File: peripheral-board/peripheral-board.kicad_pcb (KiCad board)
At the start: 2 copper layers, 165 x 130 mm, 261 parts, among them CON4001 BARREL_JACK, CON8001 SD_Card, J10001 DB15_FEMALE_HighDensity, J7001 FCR1295, P10001 VGA, P1001 Peripheral Bus, P1002 Power, Q4001 IRLML2244TRPbF, Q5001 IRLML2244TRPbF, Q5002 IRLML2244TRPbF, Q8001 BSS84LT1G, SW1001 Power, SW2001 1, SW2002 2, SW2003 3, SW2004 4, SW2005 5, SW2006 6, SW2007 7, SW2008 8, SW2009 9, SW2010 0, SW2011 +, SW2012 ´, SW2013 BKSP, SW2014 TROLL, SW2015 §, SW2016 UP, SW2017 RMB, SW2018 Q, SW2019 W, SW2020 E, SW2021 R, SW2022 T, SW2023 Y, SW2024 U, SW2025 I, SW2026 O, SW2027 P, SW2028 Å, SW2029 ¨, SW2030 RETURN, SW2031 ALT_GR, SW2032 <, SW2033 LEFT, SW2034 MMB, SW2035 A, SW2036 S, SW2037 D, SW2038 F, SW2039 G, SW2040 H, SW2041 J, SW2042 K, SW2043 L, SW2044 Ö, SW2045 Ä, SW2046 ', SW2047 ESC, SW2048 TAB, SW2049 ALT, SW2050 DOWN, SW2051 LMB, SW2052 SHIFT_L, SW2053 Z, SW2054 X, SW2055 C, SW2056 V, SW2057 B, SW2058 N, SW2059 M, SW2060 ,, SW2061 ., SW2062 -, SW2063 SHIFT_R, SW2064 FN_R, SW2065 SPACE, SW2066 FN_L, SW2067 RIGHT, SW2068 CTRL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

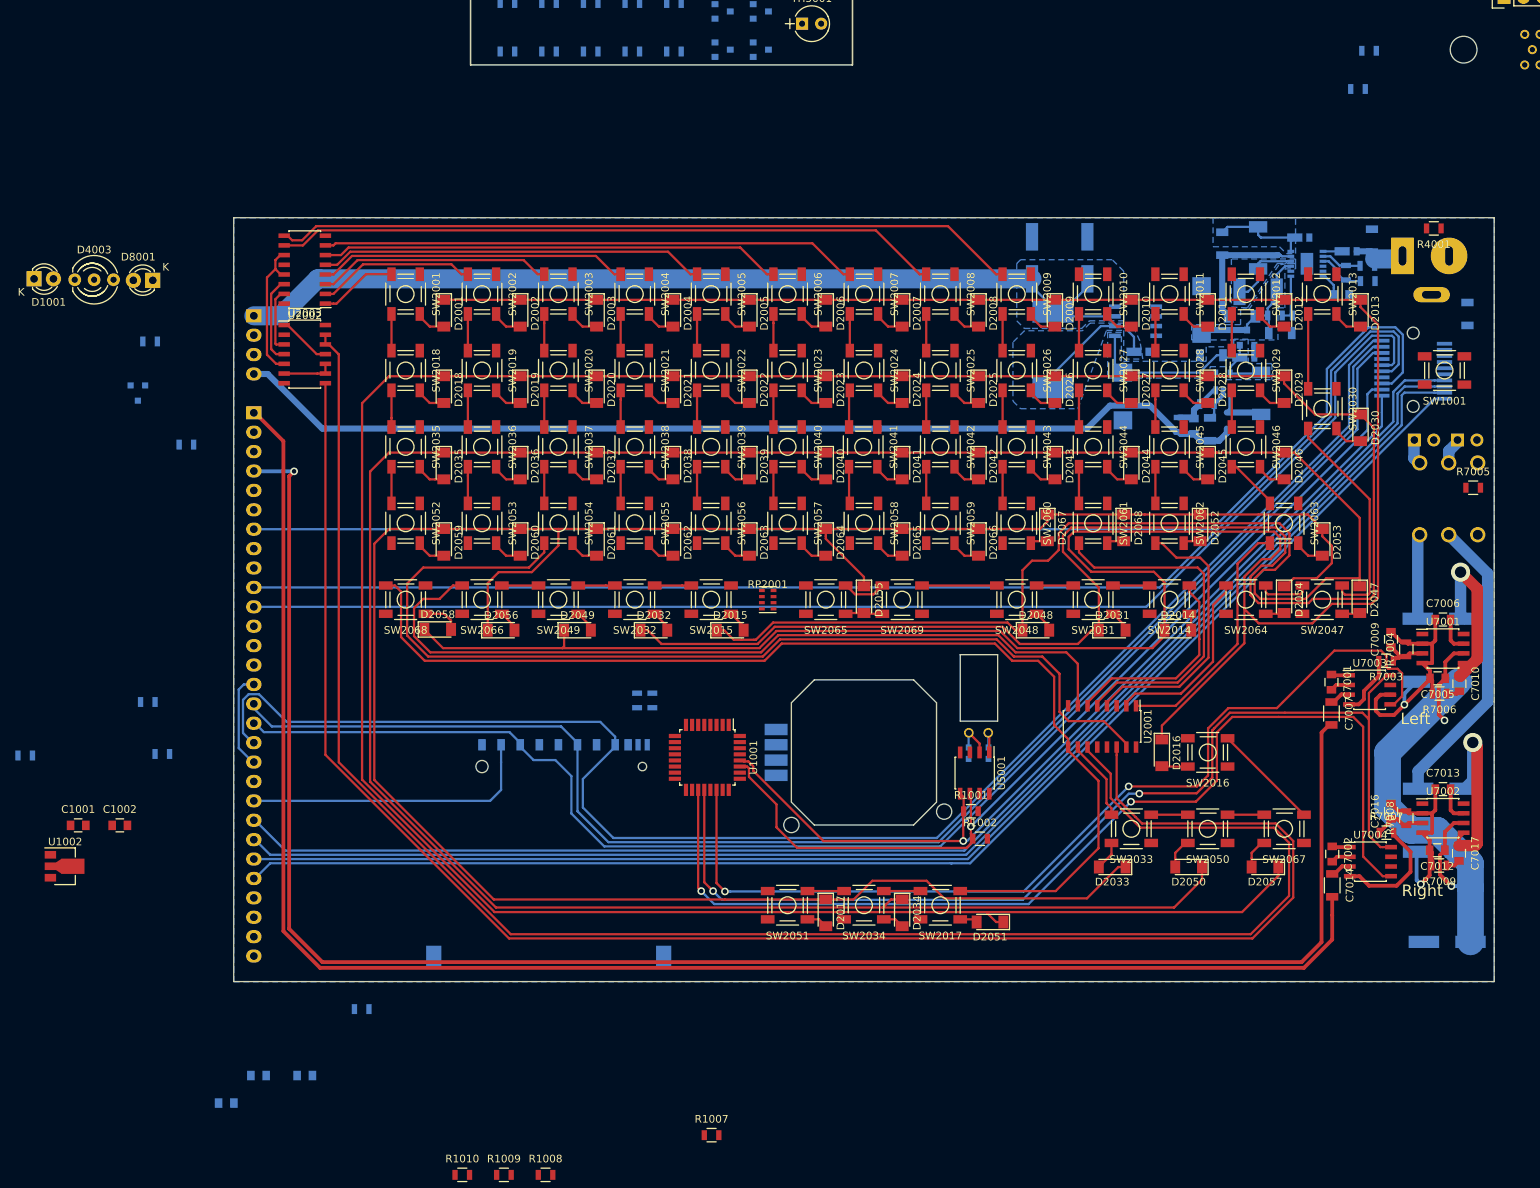
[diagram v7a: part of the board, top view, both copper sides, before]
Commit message: routed misc signals to micro
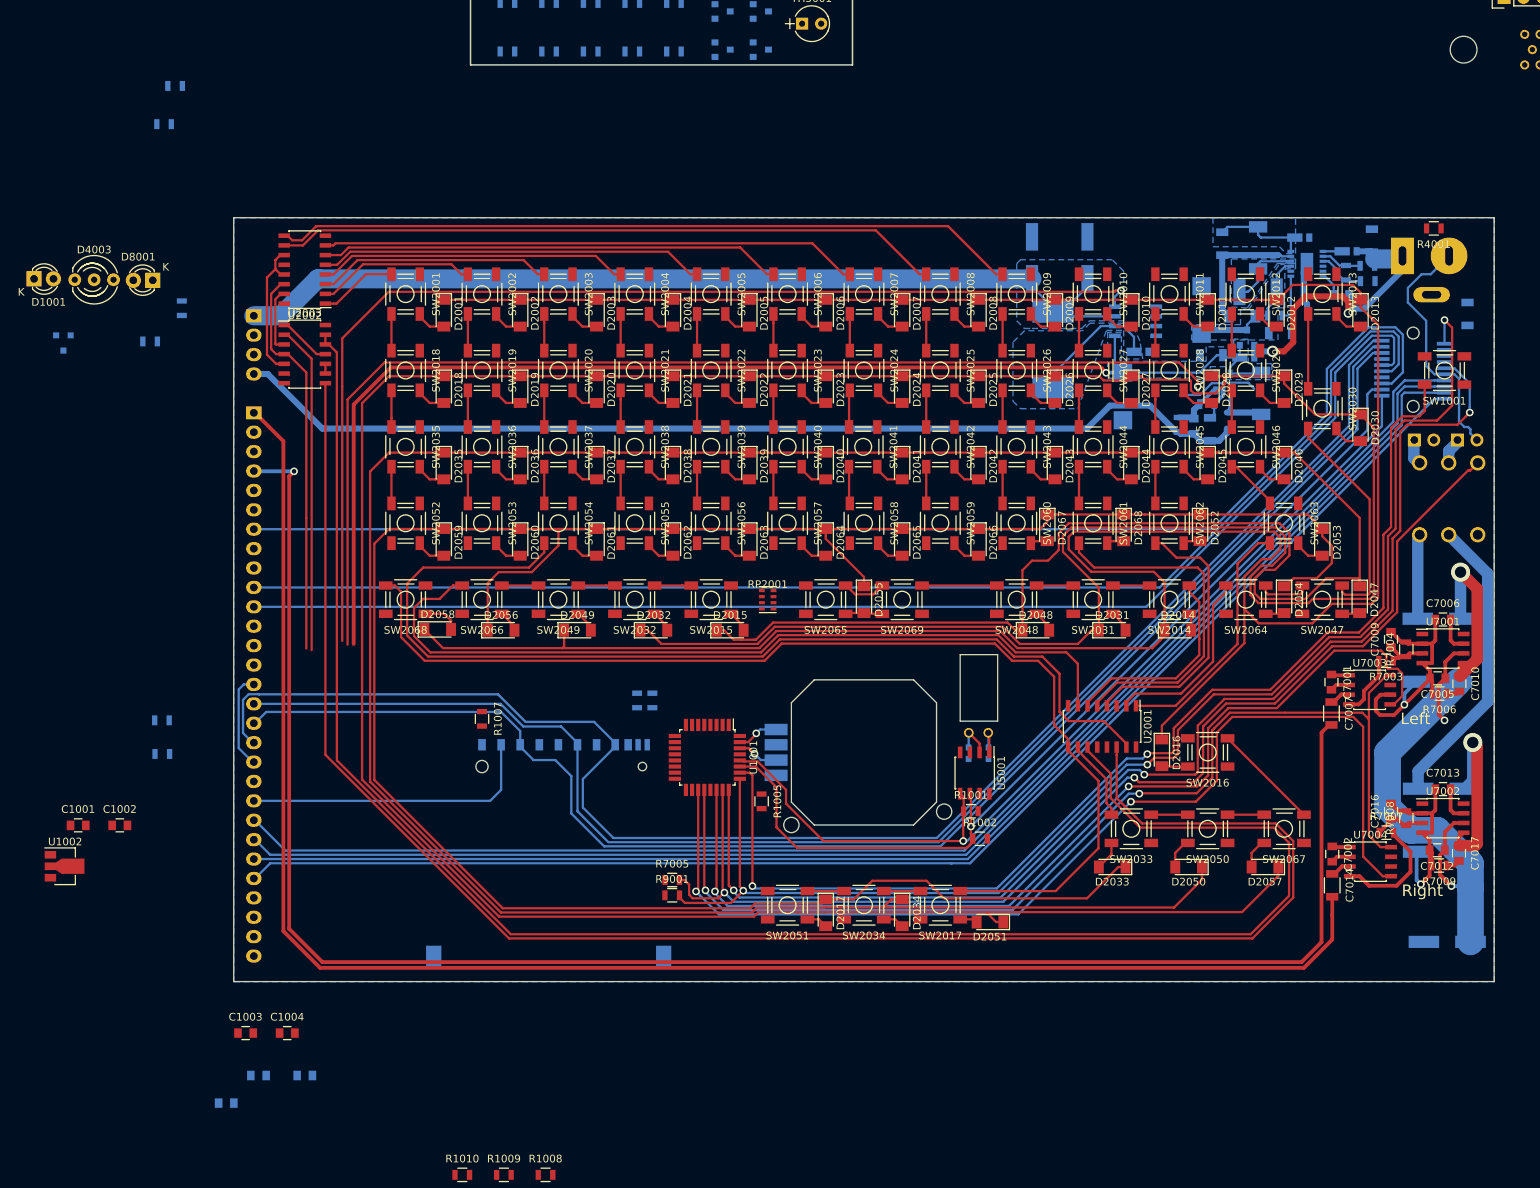
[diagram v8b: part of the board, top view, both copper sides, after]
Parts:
- added C1003: 100n, Capacitors_SMD:C_0805, F.Cu at (86.6, 156.7)
- added C1004: 100n, Capacitors_SMD:C_0805, F.Cu at (92.0, 156.7)
- R1005, R9001: moved to F.Cu
- moved R4003 156.4 mm to (77.3, 32.8)
- moved R4004 156.4 mm to (75.9, 37.8)
- moved R7005 116.7 mm to (142.4, 136.7)
- moved R1005 96.6 mm to (154.1, 126.4), turned to 270 degrees
- moved R1007 62.2 mm to (117.5, 115.6), turned to 270 degrees
- moved R9001 43.3 mm to (142.4, 138.7)
- moved R8003 17.9 mm to (78.2, 61.9), turned to 90 degrees
- moved Q8001 11.7 mm to (62.7, 66.4)
- moved R1004 3.03 mm to (75.6, 115.8)
- moved D2012 1.00 mm to (221.5, 62.5)
- moved D2028 0.50 mm to (213.0, 72.5)
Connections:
- R9001 pad 2: Net-(R9001-Pad2) -> /EXT_DET
- U1001 pad 24: /PWR_BTN -> /EXT_AN
- U1001 pad 26: /EXT_AN -> /PWR_BTN
- U1001 pad 30: /MOUSE_X -> /MOUSE_Y
- U1001 pad 31: /MOUSE_Y -> /MOUSE_X
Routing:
- net /EXT_DET: track 0.00 -> 173.5 mm, vias 0 -> 3
- net /EXT_AN: track 0.00 -> 161.7 mm, vias 0 -> 3
- net /AUD_DET: track 0.00 -> 153.9 mm, vias 0 -> 2
- net /PWR_SHDN_24: track 0.00 -> 150.2 mm, vias 0 -> 1
- net /PWR_BTN: track 0.00 -> 148.8 mm, vias 0 -> 2
- net /PWR_SHDN_3: track 0.00 -> 146.6 mm, vias 0 -> 1
- net VAA: track 102.2 -> 236.6 mm, vias 2 -> 3
- net GND: track 84.3 -> 139.6 mm
- net /KBD_RST: track 0.45 -> 43.0 mm
- net /KBD_CLK: track 12.3 -> 52.4 mm
- net +12V: track 9.40 -> 40.3 mm, vias 0 -> 2
- net /KBD_Q1: track 476.8 -> 482.7 mm
- net /MOUSE_X: track 0.00 -> 5.49 mm, vias 0 -> 1
- net Net-(U2003-Pad10): track 7.12 -> 1.72 mm
- net /MOUSE_Y: track 0.00 -> 5.39 mm, vias 0 -> 1
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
